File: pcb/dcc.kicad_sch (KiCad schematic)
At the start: 25 parts, among them U3 LM339, U4 LM339, U5 LM339, U6 LM339, U7 4052

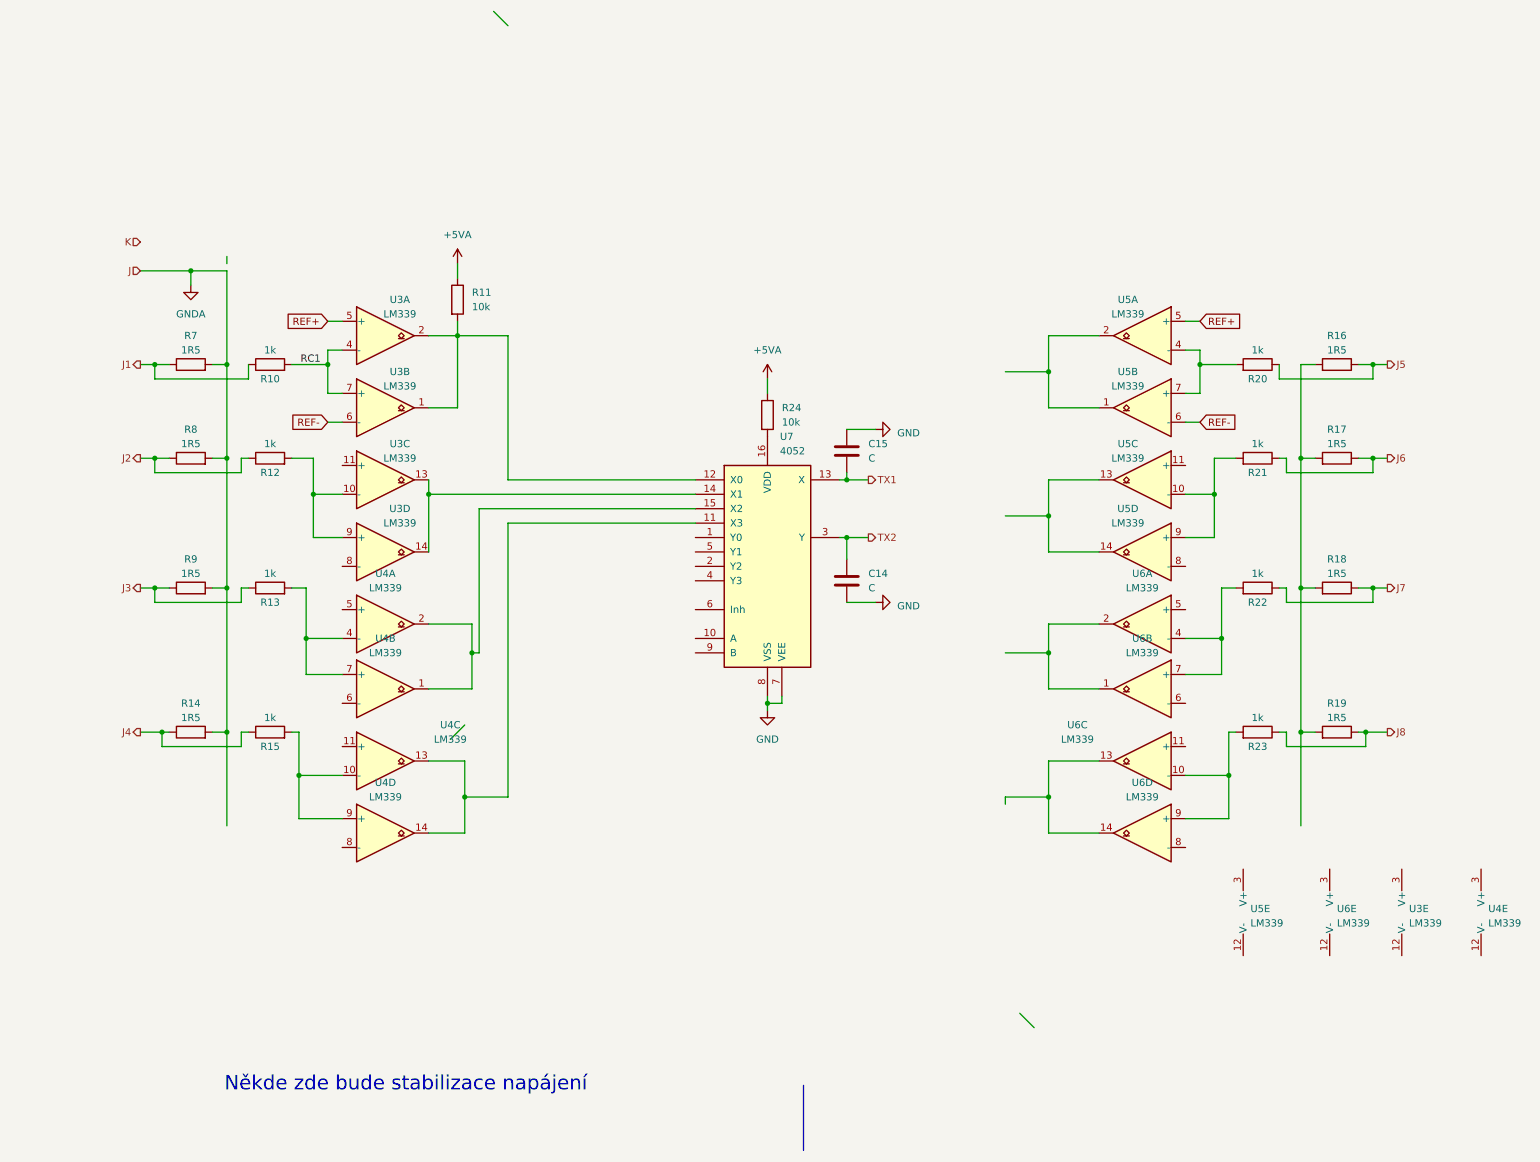
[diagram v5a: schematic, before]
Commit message: Some changes in dcc part.
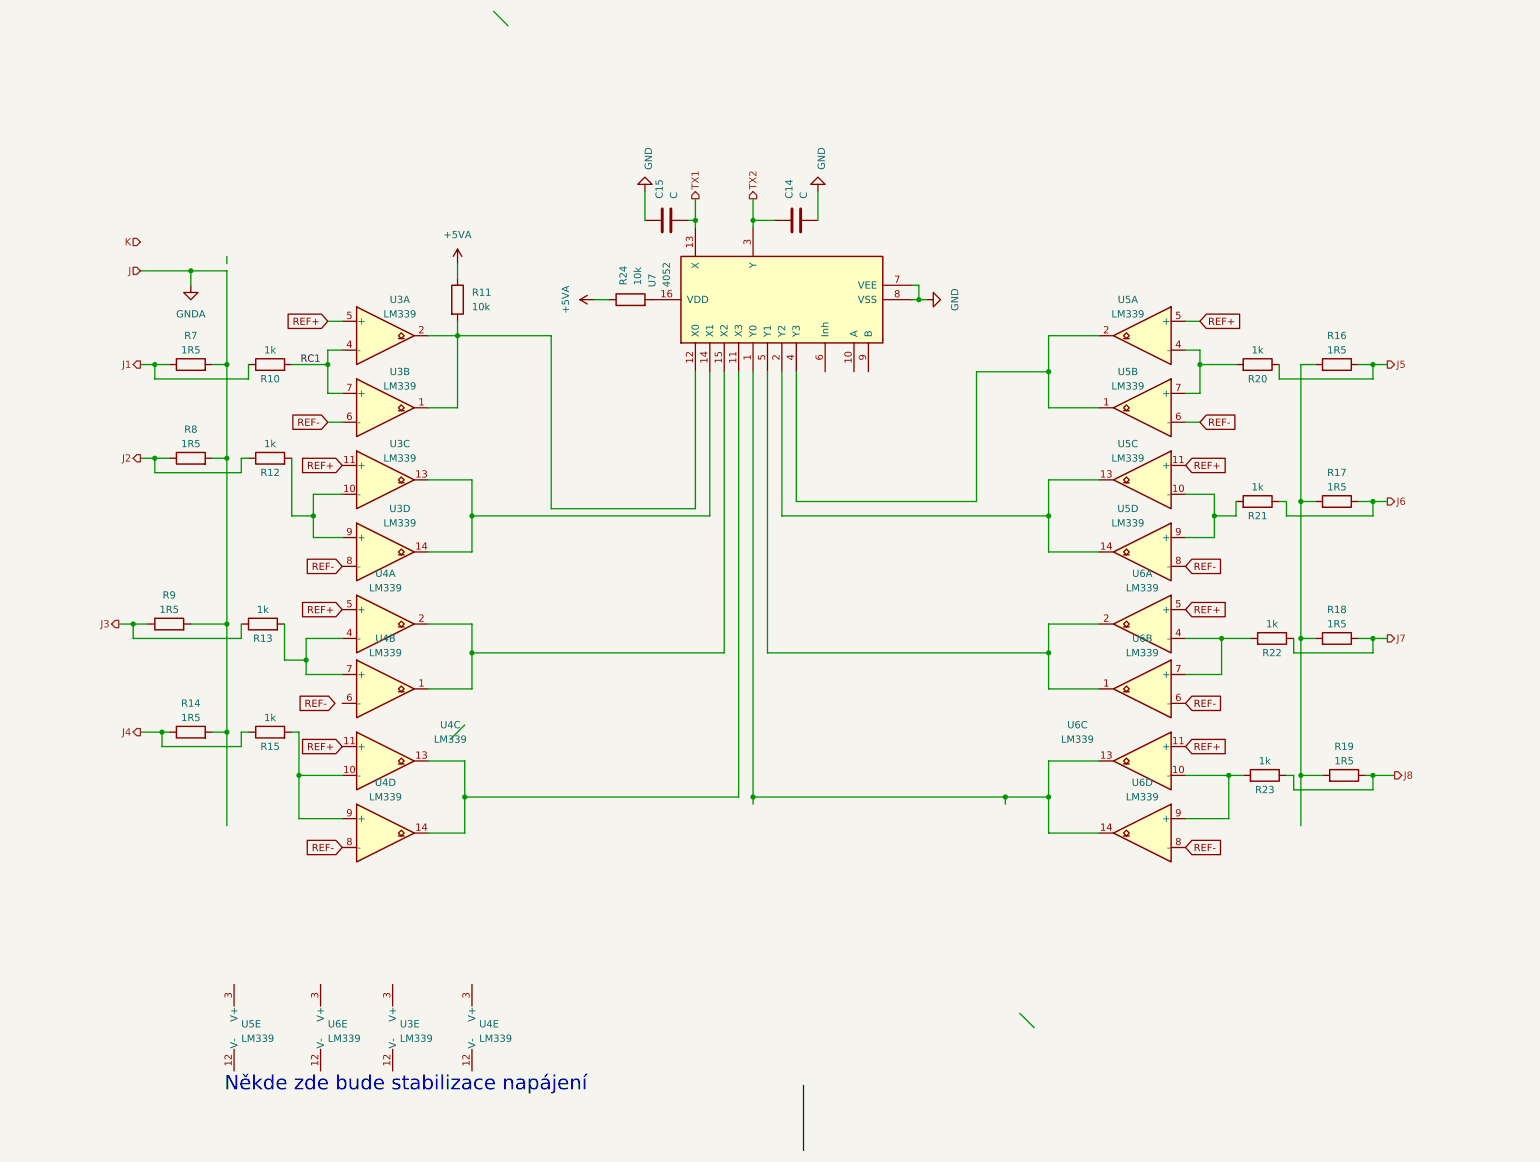
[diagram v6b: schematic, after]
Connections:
- net REF+: now also U3.11 (+), U4.11 (+), U4.5 (+), U5.11 (+), U6.11 (+), U6.5 (+)
- net REF-: now also U3.8 (-), U4.8 (-), U5.8 (-), U6.6 (-), U6.8 (-)
- net at U5.1, U5.2: now also U7.4 (Y3)
- net at U5.13, U5.14: now also U7.2 (Y2)
- net at U6.13, U6.14: now also U7.1 (Y0)
- net at U6.1, U6.2: now also U7.5 (Y1)
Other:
- moved on the sheet: C14, C15, R13, R17, R18, R19, R21, R22, R23, R24, R9, U3E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

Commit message: Added power stabilization in DCC.
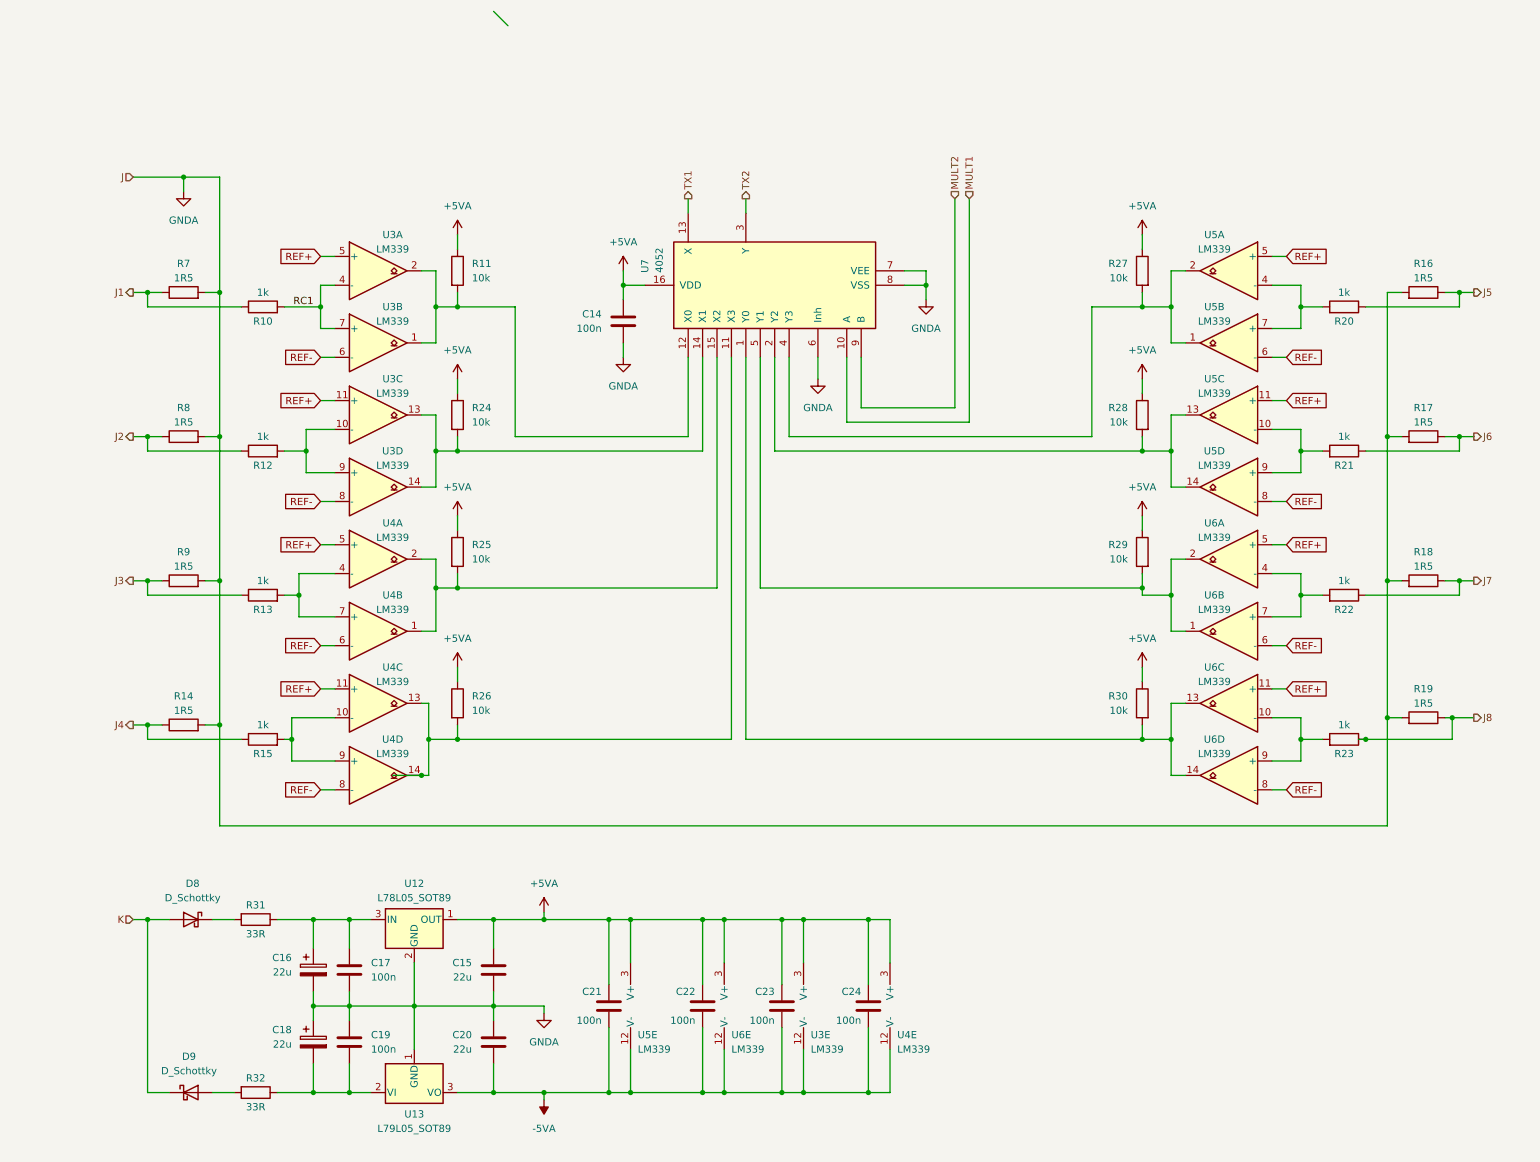
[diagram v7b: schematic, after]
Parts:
- added C16, C18: 22u, symbol Device:C_Polarized
- added C17, C19, C21, C22, C23, C24: 100n, symbol Device:C
- added C20: 22u, symbol Device:C
- added D8, D9: D_Schottky, symbol Device:D_Schottky
- added R25, R26, R27, R28, R29, R30: 10k, symbol Device:R
- added R31, R32: 33R, symbol Device:R
- added U12: L78L05_SOT89, Package_TO_SOT_SMD:SOT-89-3, symbol Regulator_Linear:L78L05_SOT89
- added U13: L79L05_SOT89, Package_TO_SOT_SMD:SOT-89-3, symbol Regulator_Linear:L79L05_SOT89
- C14: value C -> 100n
- C15: value C -> 22u
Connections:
- net +5VA: now also C14.1, C15.1, U3.3 (V+), U4.3 (V+), U5.3 (V+), U6.3 (V+), U7.16 (VDD), C21.1, C22.1, C23.1, C24.1, R25.1, R26.1, R27.1, R28.1, R29.1, R30.1, U12.1 (OUT)
- net GNDA: now also C14.2, C15.2, R16.2, R17.2, R18.2, R19.2, U7.6 (Inh), U7.7 (VEE), U7.8 (VSS), C16.2, C17.2, C18.1, C19.1, C20.1, U12.2 (GND), U13.1 (GND)
- net K: now also D8.2 (A), D9.1 (K)
- net REF-: now also U4.6 (-)
- net TX1: no longer C15.2
- net TX2: no longer C14.1
- net at U4.1, U4.2, U7.15 (X2): now also R25.2
- net -5VA: now reaches U5.12 (V-)
- net -5VA: now also U3.12 (V-), U4.12 (V-), U6.12 (V-), C20.2, C21.2, C22.2, C23.2, C24.2, U13.3 (VO)
- net at R24.2: now also U3.13, U3.14, U7.14 (X1); no longer U7.16 (VDD)
- net at U5.1, U5.2, U7.4 (Y3): now also R27.2
- net at U5.13, U5.14, U7.2 (Y2): now also R28.2
- net at U6.13, U6.14, U7.1 (Y0): now also R30.2
- net at U4.13, U4.14, U7.11 (X3): now also R26.2
- net at U6.1, U6.2, U7.5 (Y1): now also R29.2
- net MULT1: now reaches U7.10 (A)
- net MULT2: now reaches U7.9 (B)
- removed net GND: C14.2, C15.1, U7.7 (VEE), U7.8 (VSS)
- new net: C18.2, C19.2, R32.1, U13.2 (VI)
- new net: D9.2 (A), R32.2
- new net: C16.1, C17.1, R31.1, U12.3 (IN)
- new net: D8.1 (K), R31.2
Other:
- note removed: "Někde zde bude stabilizace napájení"
- moved on the sheet: R10, R11, R12, R13, R14, R15, R16, R17, R18, R19, R20, R21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

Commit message: Finished DCC part.
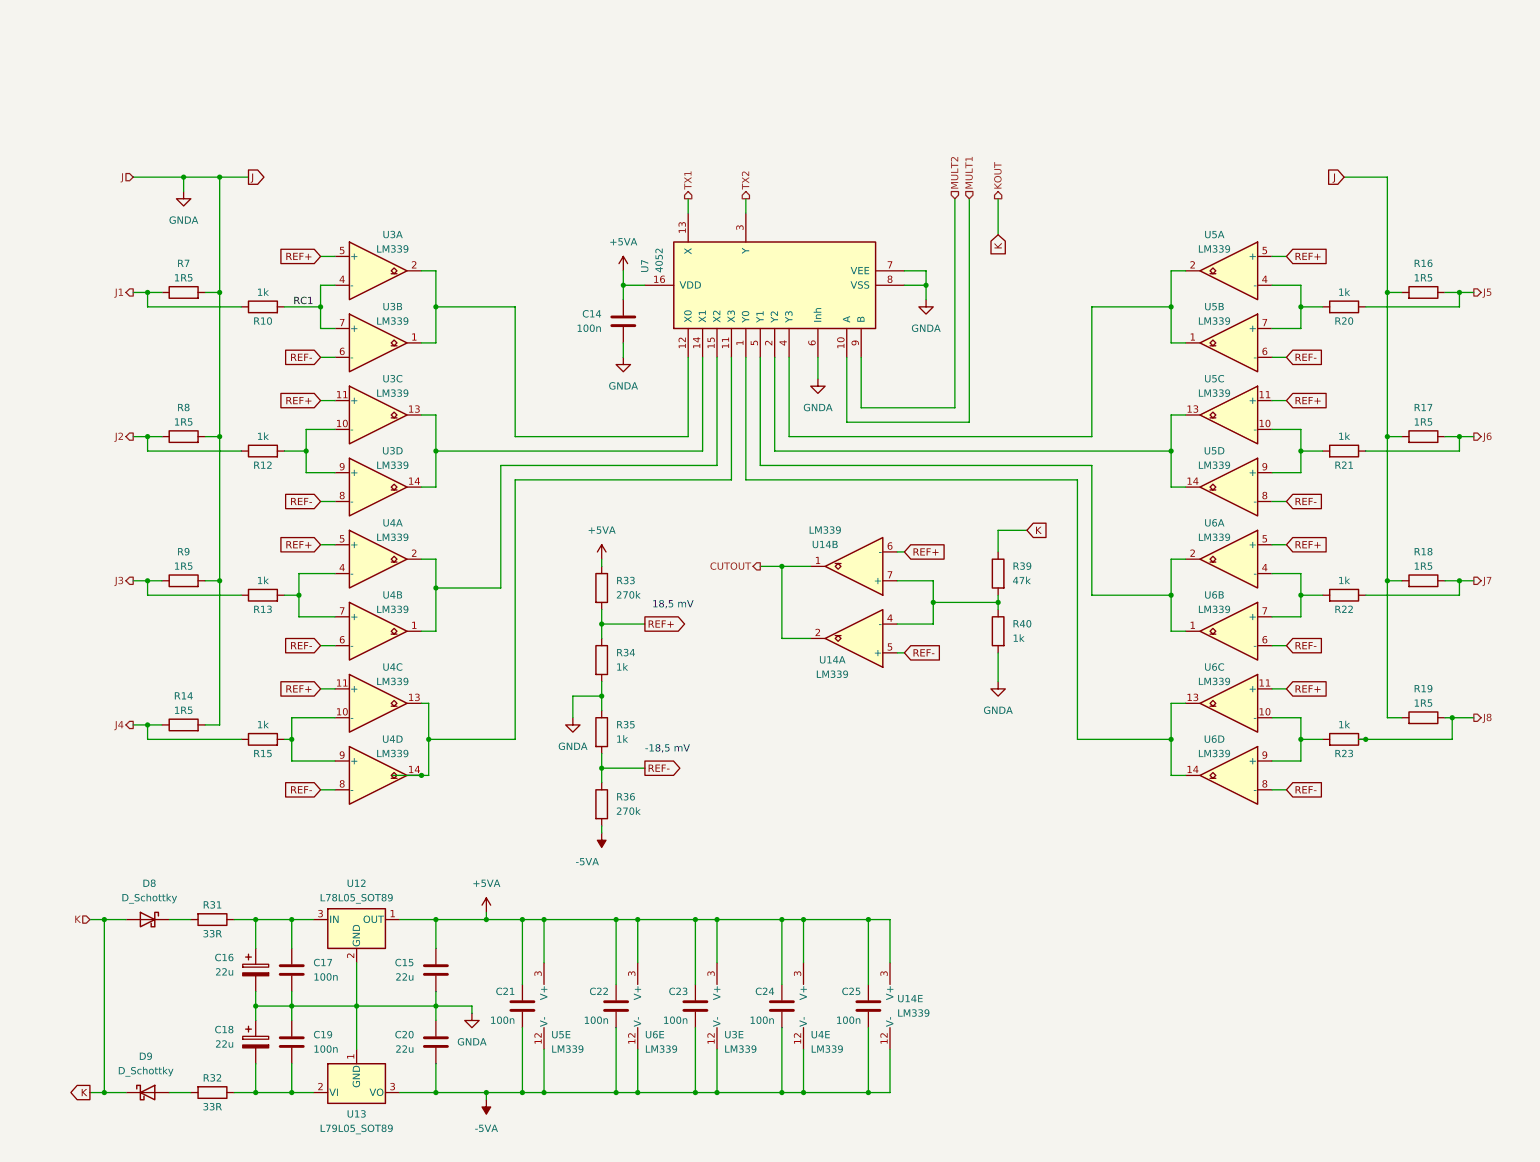
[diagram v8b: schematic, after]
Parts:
- removed R11, R24, R25, R26, R27, R28, R29, R30: 10k, symbol Device:R
- added C25: 100n, symbol Device:C
- added R33, R36: 270k, symbol Device:R
- added R34, R35, R40: 1k, symbol Device:R
- added R39: 47k, symbol Device:R
- added U14: LM339, symbol Comparator:LM339
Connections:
- net +5VA: now also C25.1, R33.1, U14.3 (V+)
- net -5VA: now also C25.2, R36.2, U14.12 (V-)
- net GNDA: now also R34.2, R35.1, R40.2
- net K: now also R39.1
- net REF+: now also R33.2, R34.1, U14.6 (-)
- net REF-: now also R35.2, R36.1, U14.5 (+)
- new net: R39.2, R40.1, U14.4 (-), U14.7 (+)
- new net CUTOUT: U14.1, U14.2
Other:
- note added: "-18,5 mV"
- note added: "18,5 mV"
- moved on the sheet: C15, C16, C17, C18, C19, C20, C21, C22, C23, C24, D8, D9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
